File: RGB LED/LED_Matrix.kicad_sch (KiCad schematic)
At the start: 64 parts

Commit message: added footprints
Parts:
- D1, D10, D11, D12, D13, D14, D15, D16, D17, D18, D19, D2, D20, D21, D22, D23, D24, D25, D26, D27, D28, D29, D3, D30, D31, D32, D33, D34, D35, D36, D37, D38, D39, D4, D40, D41, D42, D43, D44, D45, D46, D47, D48, D49, D5, D50, D51, D52, D53, D54, D55, D56, D57, D58, D59, D6, D60, D61, D62, D63, D64, D7, D8, D9: footprint (none) -> LED_SMD:LED_0603_1608Metric

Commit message: started layout
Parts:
- D1, D2, D3, D4, D5, D6, D7, D8: value LED -> Green LED
- D10, D11, D12, D13, D14, D15, D16, D9: value LED -> Dark Blue LED
- D17, D19, D21, D23, D25, D27, D29, D31: value LED -> White LED
- D18, D20, D22, D24, D26, D28, D30, D32: value LED -> Purple LED
- D33, D37, D41, D45, D49, D53, D57, D61: value LED -> Red LED
- D34, D38, D42, D46, D50, D54, D58, D62: value LED -> Orange LED
- D35, D39, D43, D47, D51, D55, D59, D63: value LED -> Yellow LED
- D36, D40, D44, D48, D52, D56, D60, D64: value LED -> Light Blue LED

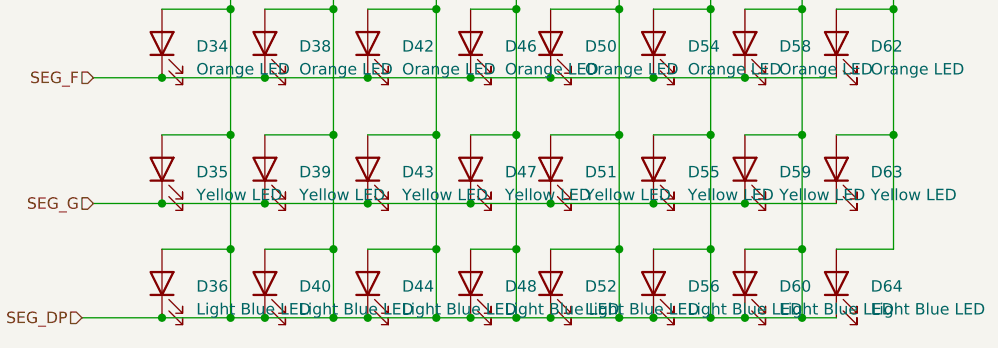
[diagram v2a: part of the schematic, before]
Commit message: changed layout, added traces/vias
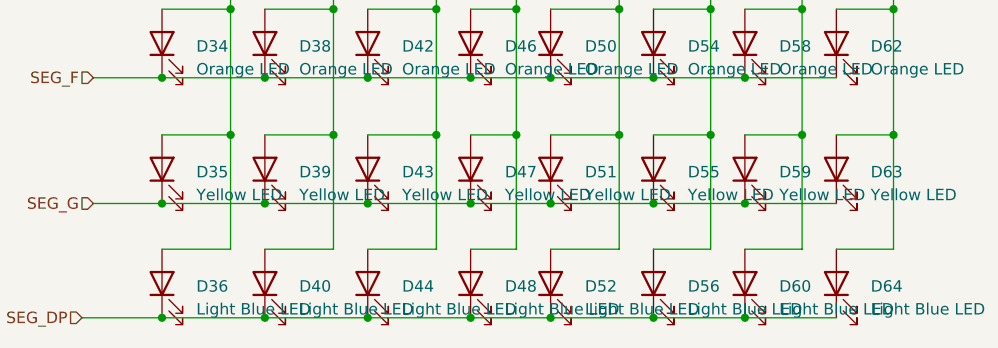
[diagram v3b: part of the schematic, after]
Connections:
- net DIG_0: no longer D10.2 (A), D11.2 (A), D12.2 (A), D13.2 (A), D14.2 (A), D15.2 (A), D19.2 (A), D2.2 (A), D20.2 (A), D21.2 (A), D22.2 (A), D23.2 (A), D24.2 (A), D25.2 (A), D26.2 (A), D27.2 (A), D28.2 (A), D29.2 (A), D3.2 (A), D30.2 (A), D36.1 (K), D37.2 (A), D38.2 (A), D39.2 (A), D4.2 (A), D40.1 (K), D40.2 (A), D41.2 (A), D42.2 (A), D43.2 (A), D44.1 (K), D44.2 (A), D45.2 (A), D46.2 (A), D47.2 (A), D48.1 (K), D48.2 (A), D49.2 (A), D5.2 (A), D50.2 (A), D51.2 (A), D52.1 (K), D52.2 (A), D53.2 (A), D54.2 (A), D55.2 (A), D56.1 (K), D56.2 (A), D57.2 (A), D58.2 (A), D59.2 (A), D6.2 (A), D60.1 (K), D60.2 (A), D64.1 (K), D7.2 (A)
- new net DIG_1: D10.2 (A), D19.2 (A), D2.2 (A), D20.2 (A), D37.2 (A), D38.2 (A), D39.2 (A), D40.2 (A)
- new net DIG_2: D11.2 (A), D21.2 (A), D22.2 (A), D3.2 (A), D41.2 (A), D42.2 (A), D43.2 (A), D44.2 (A)
- new net DIG_3: D12.2 (A), D23.2 (A), D24.2 (A), D4.2 (A), D45.2 (A), D46.2 (A), D47.2 (A), D48.2 (A)
- new net DIG_4: D13.2 (A), D25.2 (A), D26.2 (A), D49.2 (A), D5.2 (A), D50.2 (A), D51.2 (A), D52.2 (A)
- new net DIG_5: D14.2 (A), D27.2 (A), D28.2 (A), D53.2 (A), D54.2 (A), D55.2 (A), D56.2 (A), D6.2 (A)
- new net DIG_6: D15.2 (A), D29.2 (A), D30.2 (A), D57.2 (A), D58.2 (A), D59.2 (A), D60.2 (A), D7.2 (A)
- new net SEG_DP: D36.1 (K), D40.1 (K), D44.1 (K), D48.1 (K), D52.1 (K), D56.1 (K), D60.1 (K), D64.1 (K)
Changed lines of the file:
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@@
   (junction (at 88.9 101.6) (diameter 0) (color 0 0 0 0)
   )
-  (junction (at 120.65 128.27) (diameter 0) (color 0 0 0 0)
-  )
   (junction (at 88.9 36.83) (diameter 0) (color 0 0 0 0)
   )
@@
   (junction (at 124.46 44.45) (diameter 0) (color 0 0 0 0)
   )
-  (junction (at 100.33 135.89) (diameter 0) (color 0 0 0 0)
-  )
   (junction (at 135.89 96.52) (diameter 0) (color 0 0 0 0)
   )
@@
   (junction (at 104.14 109.22) (diameter 0) (color 0 0 0 0)
   )
-  (junction (at 111.76 135.89) (diameter 0) (color 0 0 0 0)
-  )
   (junction (at 92.71 83.82) (diameter 0) (color 0 0 0 0)
   )
   (junction (at 135.89 135.89) (diameter 0) (color 0 0 0 0)
   )
-  (junction (at 120.65 135.89) (diameter 0) (color 0 0 0 0)
-  )
   (junction (at 92.71 44.45) (diameter 0) (color 0 0 0 0)
   )
@@
   (junction (at 132.08 101.6) (diameter 0) (color 0 0 0 0)
   )
-  (junction (at 132.08 135.89) (diameter 0) (color 0 0 0 0)
-  )
-  (junction (at 132.08 128.27) (diameter 0) (color 0 0 0 0)
-  )
   (junction (at 124.46 83.82) (diameter 0) (color 0 0 0 0)
   )
@@
   (junction (at 162.56 49.53) (diameter 0) (color 0 0 0 0)
   )
-  (junction (at 142.24 128.27) (diameter 0) (color 0 0 0 0)
-  )
   (junction (at 100.33 115.57) (diameter 0) (color 0 0 0 0)
   )
@@
   (junction (at 100.33 76.2) (diameter 0) (color 0 0 0 0)
   )
-  (junction (at 142.24 135.89) (diameter 0) (color 0 0 0 0)
-  )
   (junction (at 92.71 57.15) (diameter 0) (color 0 0 0 0)
   )
@@
   (junction (at 115.57 96.52) (diameter 0) (color 0 0 0 0)
   )
-  (junction (at 88.9 128.27) (diameter 0) (color 0 0 0 0)
-  )
   (junction (at 81.28 109.22) (diameter 0) (color 0 0 0 0)
   )
@@
   (junction (at 132.08 76.2) (diameter 0) (color 0 0 0 0)
   )
-  (junction (at 111.76 128.27) (diameter 0) (color 0 0 0 0)
-  )
   (junction (at 115.57 123.19) (diameter 0) (color 0 0 0 0)
   )
@@
   (junction (at 142.24 76.2) (diameter 0) (color 0 0 0 0)
   )
-  (junction (at 152.4 135.89) (diameter 0) (color 0 0 0 0)
-  )
   (junction (at 135.89 109.22) (diameter 0) (color 0 0 0 0)
   )
@@
   (junction (at 115.57 109.22) (diameter 0) (color 0 0 0 0)
   )
-  (junction (at 152.4 128.27) (diameter 0) (color 0 0 0 0)
-  )
   (junction (at 81.28 135.89) (diameter 0) (color 0 0 0 0)
   )
@@
   (junction (at 88.9 115.57) (diameter 0) (color 0 0 0 0)
   )
-  (junction (at 100.33 128.27) (diameter 0) (color 0 0 0 0)
-  )
   (junction (at 115.57 57.15) (diameter 0) (color 0 0 0 0)
   )
-  (junction (at 88.9 135.89) (diameter 0) (color 0 0 0 0)
-  )
   (wire (pts (xy 104.14 109.22) (xy 92.71 109.22))
     (stroke (width 0) (type default))
@@
     (stroke (width 0) (type default))
   )
-  (wire (pts (xy 135.89 135.89) (xy 142.24 135.89))
+  (wire (pts (xy 135.89 135.89) (xy 146.05 135.89))
     (stroke (width 0) (type default))
   )
@@
     (stroke (width 0) (type default))
   )
-  (wire (pts (xy 124.46 135.89) (xy 132.08 135.89))
-    (stroke (width 0) (type default))
-  )
   (wire (pts (xy 88.9 49.53) (xy 88.9 63.5))
     (stroke (width 0) (type default))
@@
     (stroke (width 0) (type default))
   )
-  (wire (pts (xy 120.65 135.89) (xy 124.46 135.89))
-    (stroke (width 0) (type default))
-  )
   (wire (pts (xy 135.89 44.45) (xy 146.05 44.45))
     (stroke (width 0) (type default))
@@
     (stroke (width 0) (type default))
   )
-  (wire (pts (xy 146.05 135.89) (xy 152.4 135.89))
+  (wire (pts (xy 146.05 135.89) (xy 156.21 135.89))
     (stroke (width 0) (type default))
   )
@@
     (stroke (width 0) (type default))
   )
-  (wire (pts (xy 88.9 135.89) (xy 92.71 135.89))
-    (stroke (width 0) (type default))
-  )
   (wire (pts (xy 146.05 88.9) (xy 152.4 88.9))
     (stroke (width 0) (type default))
@@
     (stroke (width 0) (type default))
   )
-  (wire (pts (xy 152.4 135.89) (xy 156.21 135.89))
-    (stroke (width 0) (type default))
-  )
   (wire (pts (xy 92.71 109.22) (xy 81.28 109.22))
     (stroke (width 0) (type default))
@@
     (stroke (width 0) (type default))
   )
-  (wire (pts (xy 111.76 128.27) (xy 111.76 135.89))
-    (stroke (width 0) (type default))
-  )
   (wire (pts (xy 115.57 115.57) (xy 120.65 115.57))
     (stroke (width 0) (type default))
@@
     (stroke (width 0) (type default))
   )
-  (wire (pts (xy 104.14 135.89) (xy 111.76 135.89))
+  (wire (pts (xy 104.14 135.89) (xy 115.57 135.89))
     (stroke (width 0) (type default))
   )
@@
     (stroke (width 0) (type default))
   )
-  (wire (pts (xy 88.9 128.27) (xy 88.9 135.89))
-    (stroke (width 0) (type default))
-  )
   (wire (pts (xy 88.9 115.57) (xy 88.9 128.27))
     (stroke (width 0) (type default))
@@
     (stroke (width 0) (type default))
   )
-  (wire (pts (xy 120.65 128.27) (xy 120.65 135.89))
-    (stroke (width 0) (type default))
-  )
   (wire (pts (xy 124.46 76.2) (xy 132.08 76.2))
     (stroke (width 0) (type default))
@@
     (stroke (width 0) (type default))
   )
-  (wire (pts (xy 132.08 135.89) (xy 135.89 135.89))
+  (wire (pts (xy 124.46 135.89) (xy 135.89 135.89))
     (stroke (width 0) (type default))
   )
@@
     (stroke (width 0) (type default))
   )
-  (wire (pts (xy 81.28 135.89) (xy 88.9 135.89))
+  (wire (pts (xy 81.28 135.89) (xy 92.71 135.89))
     (stroke (width 0) (type default))
   )
@@
     (stroke (width 0) (type default))
   )
-  (wire (pts (xy 100.33 128.27) (xy 100.33 135.89))
-    (stroke (width 0) (type default))
-  )
-  (wire (pts (xy 111.76 135.89) (xy 115.57 135.89))
-    (stroke (width 0) (type default))
-  )
   (wire (pts (xy 81.28 96.52) (xy 92.71 96.52))
     (stroke (width 0) (type default))
@@
     (stroke (width 0) (type default))
   )
-  (wire (pts (xy 100.33 135.89) (xy 104.14 135.89))
-    (stroke (width 0) (type default))
-  )
   (wire (pts (xy 142.24 49.53) (xy 142.24 63.5))
     (stroke (width 0) (type default))
   )
-  (wire (pts (xy 92.71 135.89) (xy 100.33 135.89))
+  (wire (pts (xy 92.71 135.89) (xy 104.14 135.89))
     (stroke (width 0) (type default))
   )
@@
     (stroke (width 0) (type default))
   )
-  (wire (pts (xy 152.4 128.27) (xy 152.4 135.89))
-    (stroke (width 0) (type default))
-  )
   (wire (pts (xy 132.08 63.5) (xy 132.08 76.2))
     (stroke (width 0) (type default))
@@
     (stroke (width 0) (type default))
   )
-  (wire (pts (xy 115.57 135.89) (xy 120.65 135.89))
+  (wire (pts (xy 115.57 135.89) (xy 124.46 135.89))
     (stroke (width 0) (type default))
   )
@@
     (stroke (width 0) (type default))
   )
-  (wire (pts (xy 142.24 128.27) (xy 142.24 135.89))
-    (stroke (width 0) (type default))
-  )
   (wire (pts (xy 146.05 96.52) (xy 156.21 96.52))
     (stroke (width 0) (type default))
@@
     (stroke (width 0) (type default))
   )
-  (wire (pts (xy 142.24 135.89) (xy 146.05 135.89))
-    (stroke (width 0) (type default))
-  )
   (wire (pts (xy 156.21 109.22) (xy 146.05 109.22))
     (stroke (width 0) (type default))
@@
     (stroke (width 0) (type default))
   )
-  (wire (pts (xy 132.08 128.27) (xy 132.08 135.89))
-    (stroke (width 0) (type default))
-  )
